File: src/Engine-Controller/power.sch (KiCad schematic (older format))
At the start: 23 parts, among them P1 EJ508A, U2 LM22672MRE-5.0_NOPB, U3 LMS8117AMP-3.3_NOPB

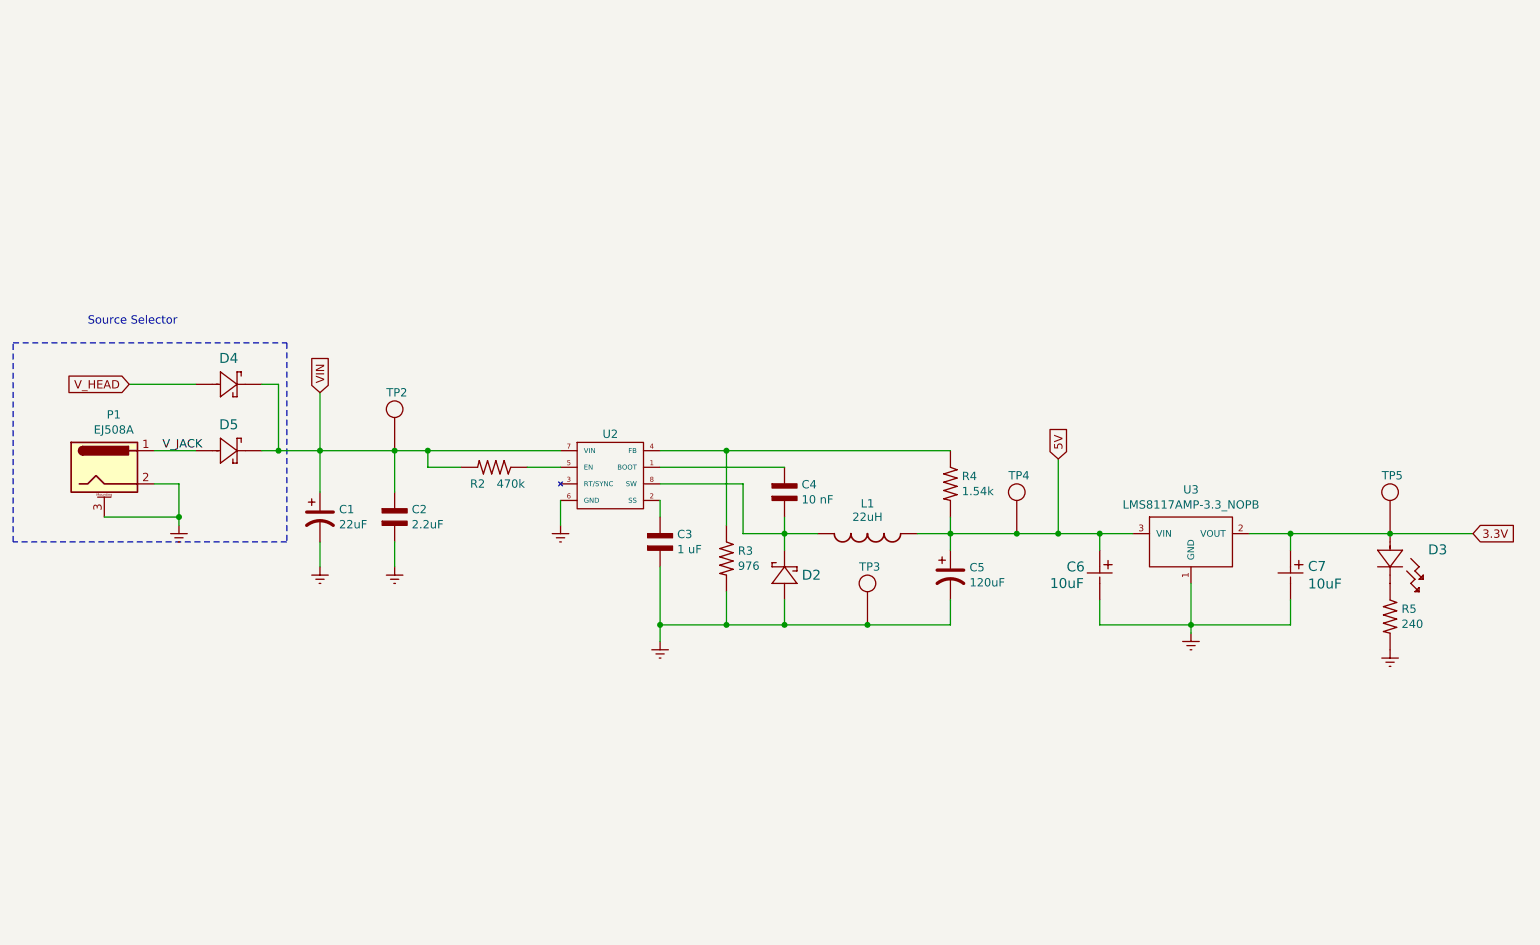
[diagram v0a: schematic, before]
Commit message: Wired 5V power multiplexor
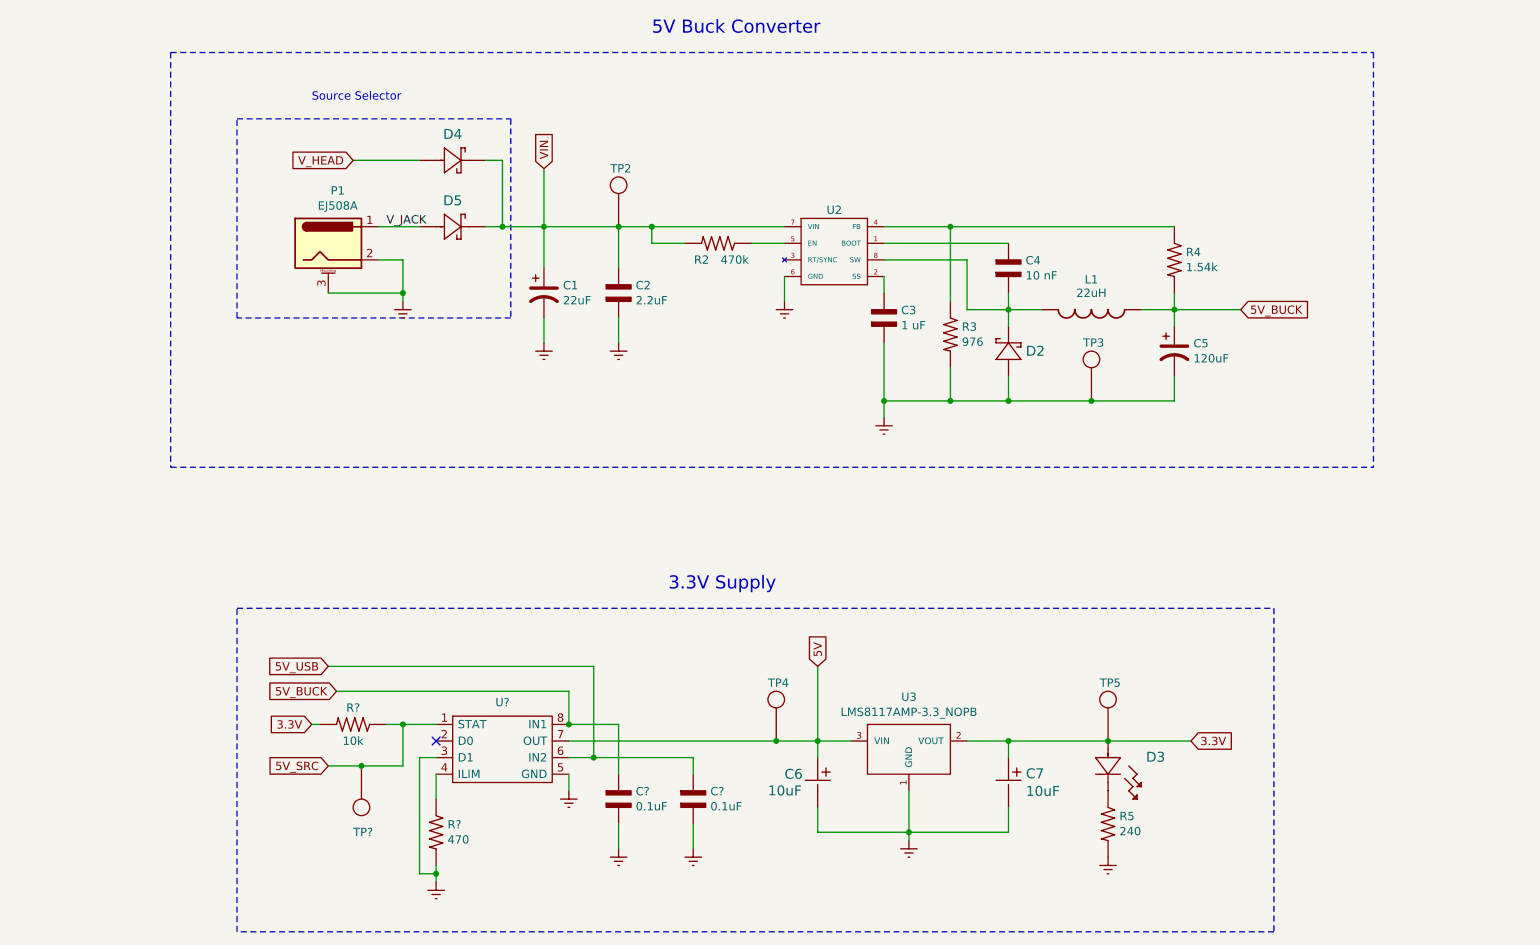
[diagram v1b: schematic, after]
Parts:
- added C? (x2): 0.1uF, symbol Engine-Controller:CAP_0603
- added R?: 470, symbol Engine-Controller:RES_0603
- added R?: 10k, symbol Engine-Controller:RES_0603
- added TP?: TP, symbol Engine-Controller:TP
- added U?: TPS2115APWR, symbol Engine-Controller:TPS2115APWR
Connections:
- net 3.3V: now also R?.2
- net 5V: now also U?.7 (OUT); no longer C5.1, L1.2, R4.2
- net Earth: now also C?.1, C?.1, R?.2, U?.3 (D1), U?.5 (GND)
- new net: R?.1, U?.4 (ILIM)
- new net 5V_BUCK: C5.1, C?.2, L1.2, R4.2, U?.8 (IN1)
- new net 5V_SRC: R?.1, TP?.1, U?.1 (STAT)
- new net 5V_USB: C?.2, U?.6 (IN2)
- no-connect marks 0 -> 1
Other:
- note added: "3.3V Supply\n"
- note added: "5V Buck Converter"
- moved on the sheet: C1, C2, C3, C4, C5, C6, C7, D2, D3, D4, D5, L1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

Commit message: Annotated 5V selector parts
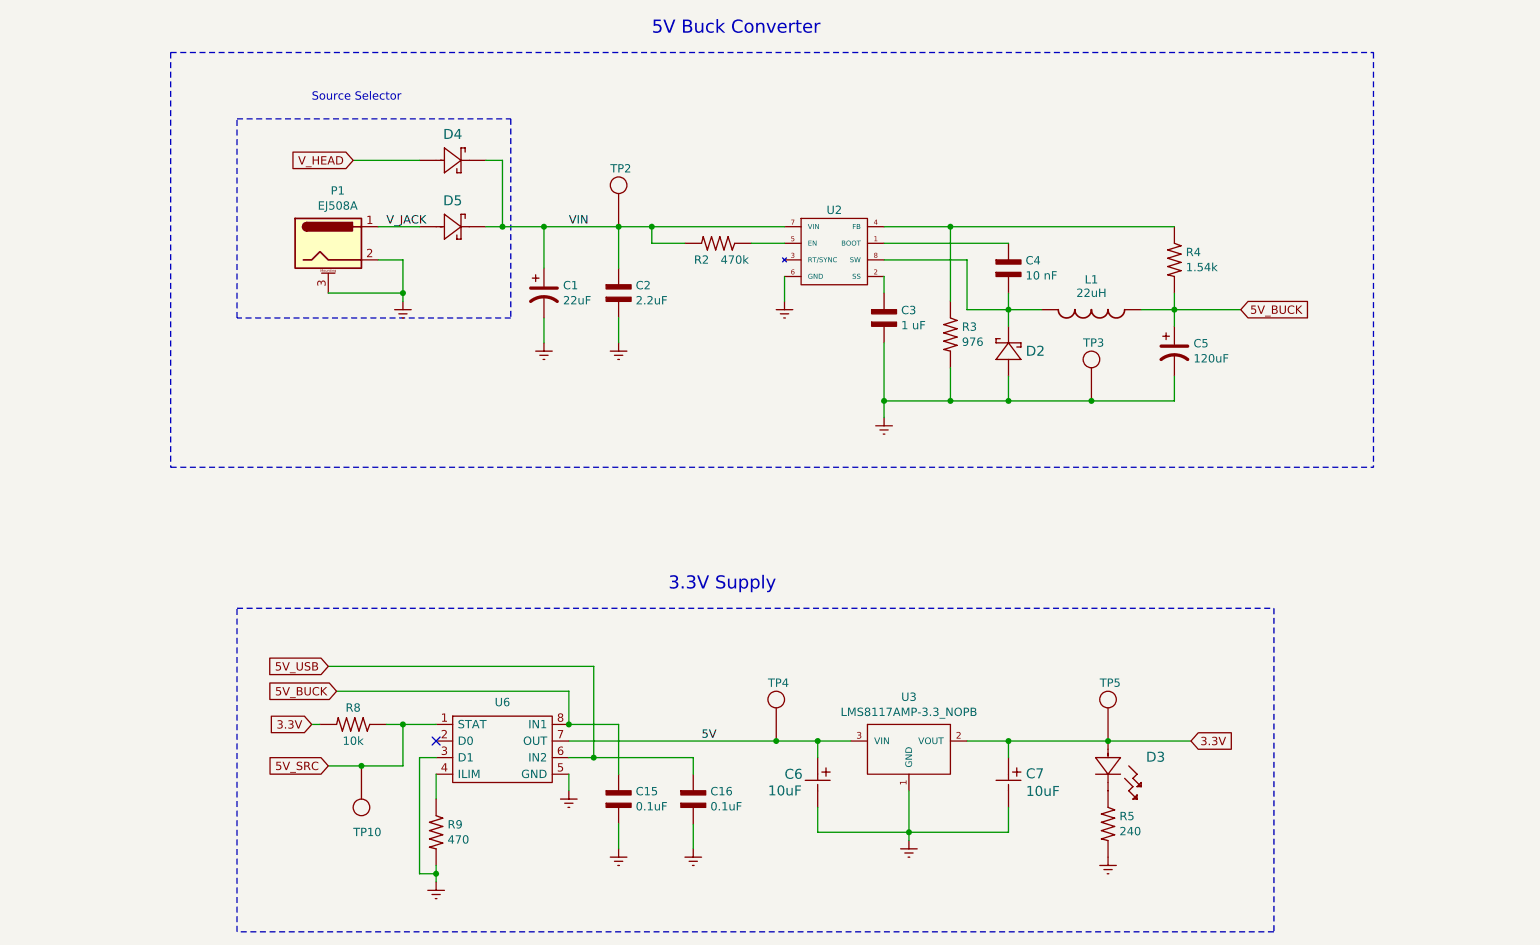
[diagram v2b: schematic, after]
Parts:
- gave numbers to parts that had none: 6
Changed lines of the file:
@@
 Wire Wire Line
 	3200 2350 3350 2350
-Text GLabel 4200 1800 1    50   Input ~ 0
-VIN
-Wire Wire Line
-	4200 1800 4200 2150
 Connection ~ 4200 2150
 $Comp
@@
 Wire Wire Line
 	6650 3200 7000 3200
-Text GLabel 5850 4800 1    50   Input ~ 0
-5V
-Wire Wire Line
-	5850 4800 5850 5250
 $Comp
 L power:Earth #PWR0108
@@
 5V Buck Converter
 $Comp
-L Engine-Controller:CAP_0603 C?
+L Engine-Controller:CAP_0603 C16
 U 1 1 60FCE9C2
 P 5100 5600
-F 0 "C?" V 5054 5703 50  0000 L CNN
+F 0 "C16" V 5054 5703 50  0000 L CNN
 F 1 "0.1uF" V 5145 5703 50  0000 L CNN
 F 2 "" H 5000 5200 50  0001 L BNN
@@
 $EndComp
 $Comp
-L Engine-Controller:CAP_0603 C?
+L Engine-Controller:CAP_0603 C15
 U 1 1 60FD414B
 P 4650 5600
-F 0 "C?" V 4604 5703 50  0000 L CNN
+F 0 "C15" V 4604 5703 50  0000 L CNN
 F 1 "0.1uF" V 4695 5703 50  0000 L CNN
 F 2 "" H 4550 5200 50  0001 L BNN
@@
 	3550 6000 3550 6050
 $Comp
-L power:Earth #PWR?
+L power:Earth #PWR08
 U 1 1 60FB68C5
 P 3550 6100
-F 0 "#PWR?" H 3550 5850 50  0001 C CNN
+F 0 "#PWR08" H 3550 5850 50  0001 C CNN
 F 1 "Earth" H 3550 5950 50  0001 C CNN
 F 2 "" H 3550 6100 50  0001 C CNN
@@
 	4500 5350 4500 4800
 $Comp
-L Engine-Controller:RES_0603 R?
+L Engine-Controller:RES_0603 R9
 U 1 1 60FACF59
 P 3550 5800
-F 0 "R?" V 3504 5869 50  0000 L CNN
+F 0 "R9" V 3504 5869 50  0000 L CNN
 F 1 "470" V 3595 5869 50  0000 L CNN
 F 2 "" H 3600 5300 50  0001 L BNN
@@
 	4350 5450 4350 5550
 $Comp
-L power:Earth #PWR?
+L power:Earth #PWR09
 U 1 1 60FA1670
 P 4350 5550
-F 0 "#PWR?" H 4350 5300 50  0001 C CNN
+F 0 "#PWR09" H 4350 5300 50  0001 C CNN
 F 1 "Earth" H 4350 5400 50  0001 C CNN
 F 2 "" H 4350 5550 50  0001 C CNN
@@
 $EndComp
 $Comp
-L Engine-Controller:TPS2115APWR U?
+L Engine-Controller:TPS2115APWR U6
 U 1 1 60F83BB7
 P 3950 5300
-F 0 "U?" H 3950 5583 50  0000 C CNN
+F 0 "U6" H 3950 5583 50  0000 C CNN
 F 1 "TPS2115APWR" H 3950 5584 50  0001 C CNN
 F 2 "" H 3800 5350 50  0001 C CNN
@@
 Connection ~ 4500 5350
 $Comp
-L power:Earth #PWR?
+L power:Earth #PWR010
 U 1 1 60FEB4E7
 P 4650 5900
-F 0 "#PWR?" H 4650 5650 50  0001 C CNN
+F 0 "#PWR010" H 4650 5650 50  0001 C CNN
 F 1 "Earth" H 4650 5750 50  0001 C CNN
 F 2 "" H 4650 5900 50  0001 C CNN
@@
 $EndComp
 $Comp
-L power:Earth #PWR?
+L power:Earth #PWR011
 U 1 1 60FEB939
 P 5100 5900
-F 0 "#PWR?" H 5100 5650 50  0001 C CNN
+F 0 "#PWR011" H 5100 5650 50  0001 C CNN
 F 1 "Earth" H 5100 5750 50  0001 C CNN
 F 2 "" H 5100 5900 50  0001 C CNN
@@
 3.3V
 $Comp
-L Engine-Controller:RES_0603 R?
+L Engine-Controller:RES_0603 R8
 U 1 1 61002496
 P 3050 5150
-F 0 "R?" H 3050 5050 50  0000 C CNN
+F 0 "R8" H 3050 5050 50  0000 C CNN
 F 1 "10k" H 3050 5250 50  0000 C CNN
 F 2 "" H 3100 4650 50  0001 L BNN
@@
 Connection ~ 5600 5250
 $Comp
-L Engine-Controller:TP TP?
+L Engine-Controller:TP TP10
 U 1 1 60F2D3F8
 P 3100 5400
-F 0 "TP?" H 3150 5800 50  0000 R CNN
+F 0 "TP10" H 3150 5800 50  0000 R CNN
 F 1 "TP" H 3022 5587 50  0001 R CNN
 F 2 "" H 3100 5400 50  0001 C CNN
@@
 Text Notes 4950 4350 0    79   ~ 0
 3.3V Supply\n
+Text Label 5150 5250 0    50   ~ 0
+5V
+Text Label 4350 2150 0    50   ~ 0
+VIN
 $EndSCHEMATC

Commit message: Connected symbols to footprints
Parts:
- C15, C16: footprint (none) -> Engine-Controller:CAP_0603
- D2: footprint SOD-123FL_MCC -> Engine-Controller:RB160VAM-60TR
- D4, D5: footprint SOD-123FL_MCC -> Engine-Controller:SM5819PL-TP
- R8, R9: footprint (none) -> Engine-Controller:RES_0603
- TP10: footprint (none) -> Engine-Controller:TP
- U6: footprint (none) -> Engine-Controller:TPS2115APWR
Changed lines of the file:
@@
 F 0 "D5" H 3650 2307 60  0000 C CNN
 F 1 "SM5819PL-TP" H 3700 1950 60  0001 C CNN
-F 2 "SOD-123FL_MCC" H 3700 1850 60  0001 C CNN
+F 2 "Engine-Controller:SM5819PL-TP" H 3700 1850 60  0001 C CNN
 F 3 "" H 3450 2150 60  0001 C CNN
 	1    3450 2150
@@
 F 0 "D4" H 3650 1907 60  0000 C CNN
 F 1 "SM5819PL-TP" H 3700 1550 60  0001 C CNN
-F 2 "SOD-123FL_MCC" H 3700 1450 60  0001 C CNN
+F 2 "Engine-Controller:SM5819PL-TP" H 3700 1450 60  0001 C CNN
 F 3 "" H 3450 1750 60  0001 C CNN
 	1    3450 1750
@@
 F 0 "D2" V 7200 2996 60  0000 R CNN
 F 1 "RB160VAM-60TR" H 7250 2900 60  0001 C CNN
-F 2 "SOD-123FL_MCC" H 7250 2800 60  0001 C CNN
+F 2 "Engine-Controller:RB160VAM-60TR" H 7250 2800 60  0001 C CNN
 F 3 "" H 7000 3100 60  0001 C CNN
 	1    7000 3100
@@
 F 0 "C16" V 5054 5703 50  0000 L CNN
 F 1 "0.1uF" V 5145 5703 50  0000 L CNN
-F 2 "" H 5000 5200 50  0001 L BNN
+F 2 "Engine-Controller:CAP_0603" H 5000 5200 50  0001 L BNN
 F 3 "" H 5050 5600 50  0001 L BNN
 	1    5100 5600
@@
 F 0 "C15" V 4604 5703 50  0000 L CNN
 F 1 "0.1uF" V 4695 5703 50  0000 L CNN
-F 2 "" H 4550 5200 50  0001 L BNN
+F 2 "Engine-Controller:CAP_0603" H 4550 5200 50  0001 L BNN
 F 3 "" H 4600 5600 50  0001 L BNN
 	1    4650 5600
@@
 F 0 "R9" V 3504 5869 50  0000 L CNN
 F 1 "470" V 3595 5869 50  0000 L CNN
-F 2 "" H 3600 5300 50  0001 L BNN
+F 2 "Engine-Controller:RES_0603" H 3600 5300 50  0001 L BNN
 F 3 "" H 3550 5800 50  0001 L BNN
 	1    3550 5800
@@
 F 0 "U6" H 3950 5583 50  0000 C CNN
 F 1 "TPS2115APWR" H 3950 5584 50  0001 C CNN
-F 2 "" H 3800 5350 50  0001 C CNN
+F 2 "Engine-Controller:TPS2115APWR" H 3800 5350 50  0001 C CNN
 F 3 "" H 3800 5350 50  0001 C CNN
 	1    3950 5300
@@
 F 0 "R8" H 3050 5050 50  0000 C CNN
 F 1 "10k" H 3050 5250 50  0000 C CNN
-F 2 "" H 3100 4650 50  0001 L BNN
+F 2 "Engine-Controller:RES_0603" H 3100 4650 50  0001 L BNN
 F 3 "" H 3050 5150 50  0001 L BNN
 	1    3050 5150
@@
 F 0 "TP10" H 3150 5800 50  0000 R CNN
 F 1 "TP" H 3022 5587 50  0001 R CNN
-F 2 "" H 3100 5400 50  0001 C CNN
+F 2 "Engine-Controller:TP" H 3100 5400 50  0001 C CNN
 F 3 "" H 3100 5400 50  0001 C CNN
 	1    3100 5400

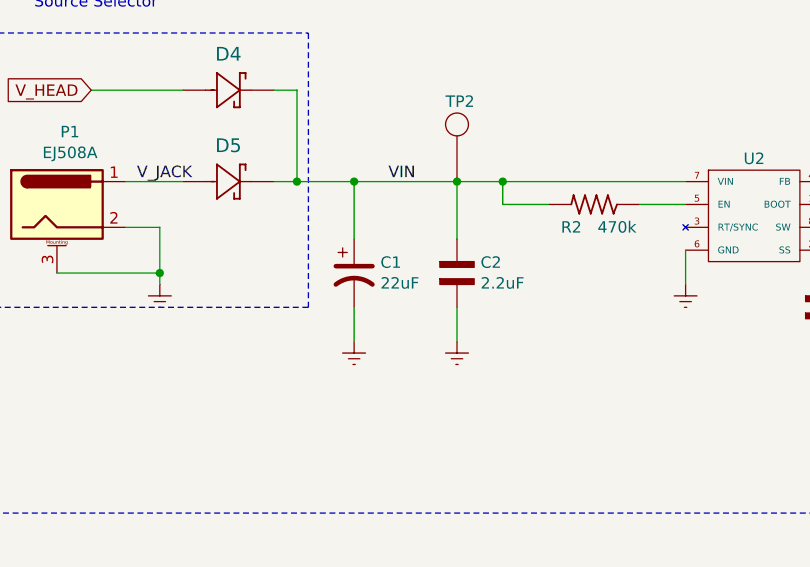
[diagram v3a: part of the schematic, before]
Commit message: Changed C1 cap
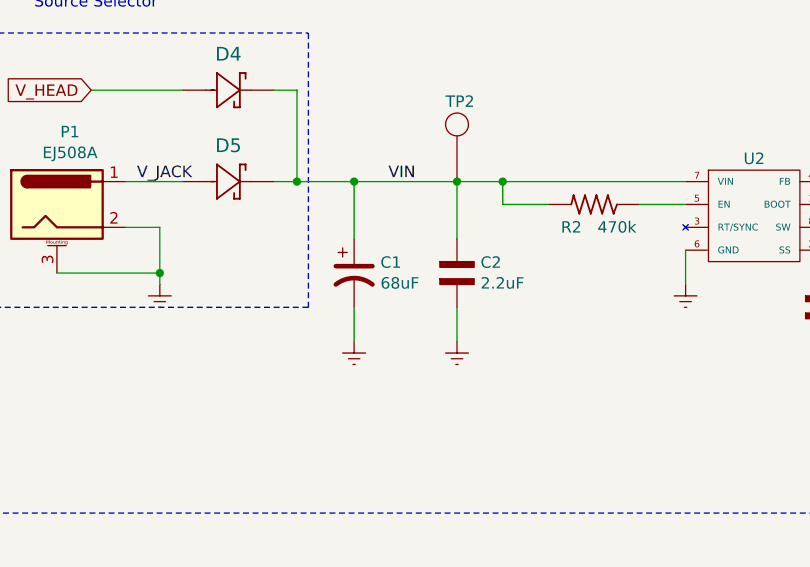
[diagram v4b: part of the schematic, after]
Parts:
- C1: value 22uF -> 68uF
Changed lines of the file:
@@
 P 4200 2550
 F 0 "C1" H 4315 2596 50  0000 L CNN
-F 1 "22uF" H 4315 2505 50  0000 L CNN
+F 1 "68uF" H 4315 2505 50  0000 L CNN
 F 2 "Engine-Controller:UKL1C220KDDANATD" H 4200 2550 50  0001 C CNN
 F 3 "~" H 4200 2550 50  0001 C CNN

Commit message: Added new C1 cap to PCB layout
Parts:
- C1: footprint Engine-Controller:UKL1C220KDDANATD -> Engine-Controller:EEEFPV680XAP
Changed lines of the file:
@@
 F 0 "C1" H 4315 2596 50  0000 L CNN
 F 1 "68uF" H 4315 2505 50  0000 L CNN
-F 2 "Engine-Controller:UKL1C220KDDANATD" H 4200 2550 50  0001 C CNN
+F 2 "Engine-Controller:EEEFPV680XAP" H 4200 2550 50  0001 C CNN
 F 3 "~" H 4200 2550 50  0001 C CNN
 	1    4200 2550

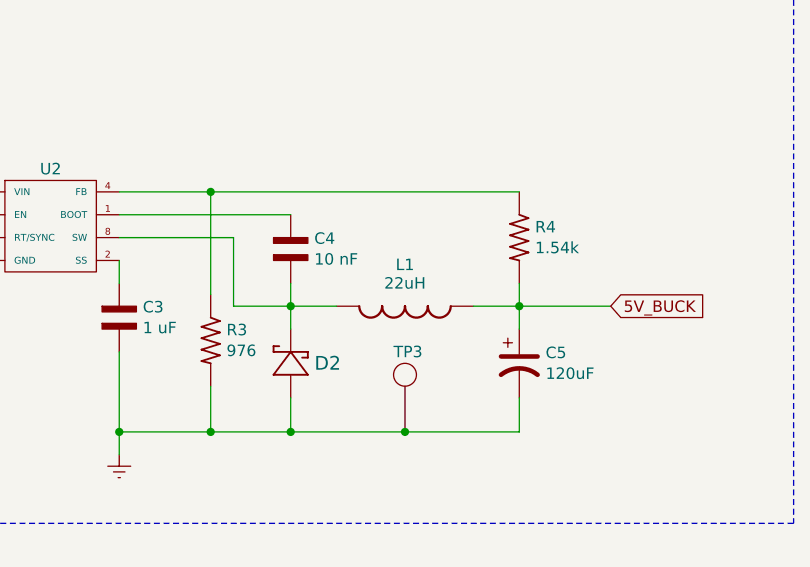
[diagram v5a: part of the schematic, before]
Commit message: Updated L1 inductor
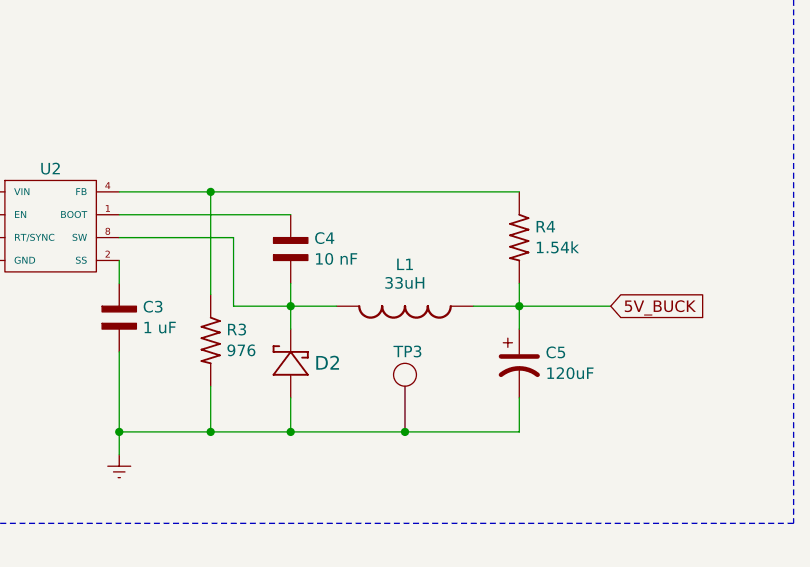
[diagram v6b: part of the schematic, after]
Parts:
- L1: value 22uH -> 33uH; footprint Engine-Controller:CBC3225T220KR -> Engine-Controller:SRP1038A-330M
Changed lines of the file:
@@
 P 7500 2650
 F 0 "L1" H 7500 2831 50  0000 C CNN
-F 1 "22uH" H 7500 2750 50  0000 C CNN
-F 2 "Engine-Controller:CBC3225T220KR" H 7350 2450 50  0001 L BNN
+F 1 "33uH" H 7500 2750 50  0000 C CNN
+F 2 "Engine-Controller:SRP1038A-330M" H 7350 2450 50  0001 L BNN
 F 3 "" H 7500 2650 50  0001 L BNN
 	1    7500 2650

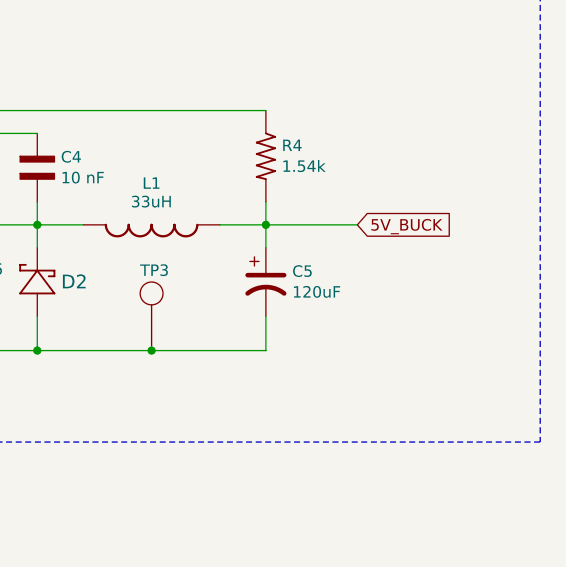
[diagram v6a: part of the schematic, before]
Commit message: Removed SWD 3.3V connections
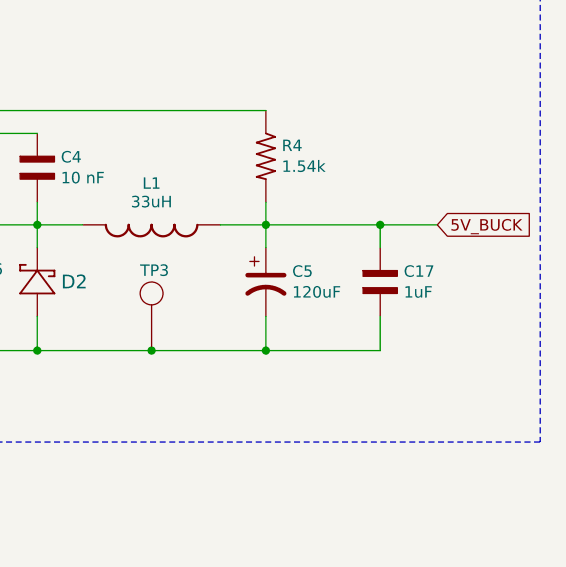
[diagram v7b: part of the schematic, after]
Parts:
- added C17: 1uF, Engine-Controller:CAP_0603, symbol Engine-Controller:CAP_0603
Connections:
- net 5V_BUCK: now also C17.2
- net Earth: now also C17.1
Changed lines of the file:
@@
 Wire Wire Line
 	3350 2350 3350 2550
-Wire Wire Line
-	8000 2650 8400 2650
 $Comp
 L Engine-Controller:TP TP4
@@
 Wire Wire Line
 	3350 2550 3350 2600
-Text GLabel 8400 2650 2    50   Input ~ 0
+Text GLabel 8750 2650 2    50   Input ~ 0
 5V_BUCK
 Wire Notes Line
@@
 Text Label 4350 2150 0    50   ~ 0
 VIN
+$Comp
+L Engine-Controller:CAP_0603 C17
+U 1 1 60FF51CA
+P 8500 2900
+F 0 "C17" V 8454 3003 50  0000 L CNN
+F 1 "1uF" V 8545 3003 50  0000 L CNN
+F 2 "Engine-Controller:CAP_0603" H 8400 2500 50  0001 L BNN
+F 3 "" H 8450 2900 50  0001 L BNN
+	1    8500 2900
+	0    1    1    0
+$EndComp
+Wire Wire Line
+	8500 3200 8000 3200
+Connection ~ 8000 3200
+Wire Wire Line
+	8000 2650 8500 2650
+Wire Wire Line
+	8500 3050 8500 3200
+Wire Wire Line
+	8500 2750 8500 2650
+Connection ~ 8500 2650
+Wire Wire Line
+	8500 2650 8750 2650
 $EndSCHEMATC
